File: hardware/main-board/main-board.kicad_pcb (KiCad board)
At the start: 4 copper layers, 77 x 38 mm, 51 parts, among them J1 USB_B_Micro, J2 STDC14, SW1 SW_Push, SW2 SW_Push, U1 TCS3472, U2 STM32L052K6U6, U3 AP2502, U4 USBLC6-2SC6, U5 RT9193

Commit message: Board layout work in progress
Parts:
- removed L1: 600 Ohm, Inductor_SMD:L_0603_1608Metric
- added C14: 1uF, Capacitor_SMD:C_0603_1608Metric, F.Cu at (102.5, 66.9)
- added C15: 1uF, Capacitor_SMD:C_0603_1608Metric, F.Cu at (100.8, 66.9)
- added C16: 1uF, Capacitor_SMD:C_0603_1608Metric, F.Cu at (99.2, 66.9)
- added C17: 1uF, Capacitor_SMD:C_0603_1608Metric, F.Cu at (97.5, 66.9)
- added C18: 0.1uF, Capacitor_SMD:C_0603_1608Metric, F.Cu at (98.0, 56.0)
- added C19: 2.2uF, Capacitor_SMD:C_0603_1608Metric, F.Cu at (86.6, 66.9)
- added C20: 4.7uF, Capacitor_SMD:C_0603_1608Metric, F.Cu at (88.3, 66.9)
- added C21: 0.1uF, Capacitor_SMD:C_0603_1608Metric, F.Cu at (106.0, 56.0)
- added C22: 0.1uF, Capacitor_SMD:C_0603_1608Metric, F.Cu at (131.1, 52.3)
- added C23: 0.1uF, Capacitor_SMD:C_0603_1608Metric, F.Cu at (136.5, 70.6)
- added D10: ESDALC6V1-1U2, lib_fp:ST0201, F.Cu at (109.0, 51.0)
- added D11: ESDALC6V1-1U2, lib_fp:ST0201, F.Cu at (140.2, 71.9)
- added D9: ESDALC6V1-1U2, lib_fp:ST0201, F.Cu at (101.0, 51.0)
- added F1: 250mA, lib_fp:BF_0ZCJ_1206, F.Cu at (134.0, 64.1)
- added FB1: 600R @ 100MHz, Inductor_SMD:L_0603_1608Metric, F.Cu at (129.5, 64.1)
- added FB2: 600R @ 100MHz, Inductor_SMD:L_0603_1608Metric, F.Cu at (163.6, 89.4)
- added J3: Display Connector, lib_fp:ER-CON30HT-1, F.Cu at (95.0, 70.0)
- added J4: Conn_01x02, Connector_JST:JST_SH_BM02B-SRSS-TB_1x02-1MP_P1.00mm_Vertical, F.Cu at (143.4, 50.8)
- added NT1: Net-Tie_2, NetTie:NetTie-2_SMD_Pad0.5mm, F.Cu at (132.5, 46.0)
- added NT2: Net-Tie_2, NetTie:NetTie-2_SMD_Pad0.5mm, F.Cu at (91.2, 67.4)
- added R10: 390K, Resistor_SMD:R_0603_1608Metric, F.Cu at (89.9, 66.9)
- added R11: 100K, Resistor_SMD:R_0603_1608Metric, F.Cu at (100.5, 49.0)
- added R12: 330R, Resistor_SMD:R_0603_1608Metric, F.Cu at (109.0, 56.0)
- added R13: 100K, Resistor_SMD:R_0603_1608Metric, F.Cu at (108.5, 49.0)
- added R14: 330R, Resistor_SMD:R_0603_1608Metric, F.Cu at (136.5, 72.1)
- added R15: 100K, Resistor_SMD:R_0603_1608Metric, F.Cu at (138.8, 71.4)
- added R9: 330R, Resistor_SMD:R_0603_1608Metric, F.Cu at (101.0, 56.0)
- added SW3: SW_Push, lib_fp:ESwitch_TL1105_6mm_H7.5mm, B.Cu at (99.0, 50.0)
- added SW4: SW_Push, lib_fp:ESwitch_TL1105_6mm_H7.5mm, B.Cu at (107.0, 50.0)
- added SW5: SW_Detect, lib_fp:CK_KSU213WLFG, F.Cu at (143.0, 69.0)
- added U6: AP2502, Package_TO_SOT_SMD:SOT-23-6, F.Cu at (130.0, 46.5)
- SW1, SW2: footprint Button_Switch_THT:SW_PUSH_6mm_H5mm -> lib_fp:ESwitch_TL1105_6mm_H7.5mm
- TP2: footprint TestPoint:TestPoint_Keystone_5005-5009_Compact -> TestPoint:TestPoint_Pad_D2.0mm
- U1: value TCS3472 -> TSL2591; footprint lib_fp:AMS_TCS3472_DFN-6 -> lib_fp:AMS_TSL2591
- moved C8 72.1 mm to (162.8, 83.1)
- moved D7 72.1 mm to (173.2, 73.7)
- moved J2 72.1 mm to (175.5, 69.2)
- moved R8 72.1 mm to (166.0, 68.5)
- moved U2 72.1 mm to (167.9, 83.7)
- moved C2 72.1 mm to (162.8, 78.6)
- moved C3 72.1 mm to (162.8, 80.5)
- moved C5 72.1 mm to (162.8, 85.0)
- moved C6 72.1 mm to (162.8, 86.9)
- moved D8 72.1 mm to (175.8, 76.1)
- moved R6 72.1 mm to (166.0, 78.6)
- moved R7 72.1 mm to (166.0, 71.8)
- moved C4 72.1 mm to (173.0, 85.8)
- moved G*** 62.2 mm to (135.1, 108.3)
- moved TP3 39.2 mm to (130.3, 89.0)
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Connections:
- J1 pad 1: +5V -> Net-(F1-Pad2)
- TP1 pad 1: +5V -> Net-(F1-Pad2)
- U1 pad 1: Net-(C1-Pad1) -> /I2C1_SCL
- U1 pad 2: /I2C1_SCL -> Net-(U1-Pad2)
- U1 pad 5: Net-(U1-Pad5) -> Net-(C1-Pad1)
- U2 pad 10: Net-(U2-Pad10) -> /DISP_~CS
- U2 pad 11: Net-(U2-Pad11) -> /DISP_SCK
- U2 pad 12: Net-(U2-Pad12) -> /DISP_D~C
- U2 pad 13: Net-(U2-Pad13) -> /DISP_MOSI
- U2 pad 14: Net-(U2-Pad14) -> /DISP_~RES
- U2 pad 18: Net-(U2-Pad18) -> /BTN5
- U2 pad 25: Net-(U2-Pad25) -> /BTN4
- U2 pad 26: /BTN1 -> /BTN3
- U2 pad 28: Net-(U2-Pad28) -> /BTN1
- U2 pad 8: Net-(U2-Pad8) -> /RLED_EN
- U2 pad 9: /LED_EN -> /TLED_EN
- U3 pad 1: /LED_EN -> /RLED_EN
- U4 pad 5: +5V -> Net-(F1-Pad2)
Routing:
- net Net-(D3-Pad1): track 56.3 -> 0.00 mm
- net /I2C1_SCL: track 60.3 -> 13.4 mm, vias 2 -> 0
- net /I2C1_SDA: track 55.6 -> 11.4 mm, vias 2 -> 0
- net Net-(D2-Pad1): track 38.5 -> 0.00 mm
- net /BTN2: track 27.6 -> 1.40 mm, vias 2 -> 0
- net /LED_EN: track 25.5 -> 0.00 mm
- net /BTN1: track 21.1 -> 1.40 mm, vias 2 -> 0
- net +5V: track 33.2 -> 14.9 mm
- net Net-(D1-Pad1): track 17.7 -> 0.00 mm
- net Net-(D4-Pad1): track 16.5 -> 0.00 mm
- net Net-(F1-Pad2): track 0.00 -> 10.6 mm
- net Net-(D9-Pad1): track 0.00 -> 9.55 mm
- net Net-(D10-Pad1): track 0.00 -> 9.55 mm
- net GND: track 40.6 -> 49.7 mm, vias 33 -> 41
- net Net-(D11-Pad1): track 0.00 -> 5.78 mm
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- removed copper zone on In2.Cu, net +3V3
- removed copper zone on In2.Cu, net +5V
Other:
- board size 77 x 38 mm -> 105 x 38 mm
- board text added: "Rev: A 2021-06-??"
- board text removed: "Reflection Densitometer Probe Development & Test Board"
- board text removed: "Rev: A 2021-03-29"

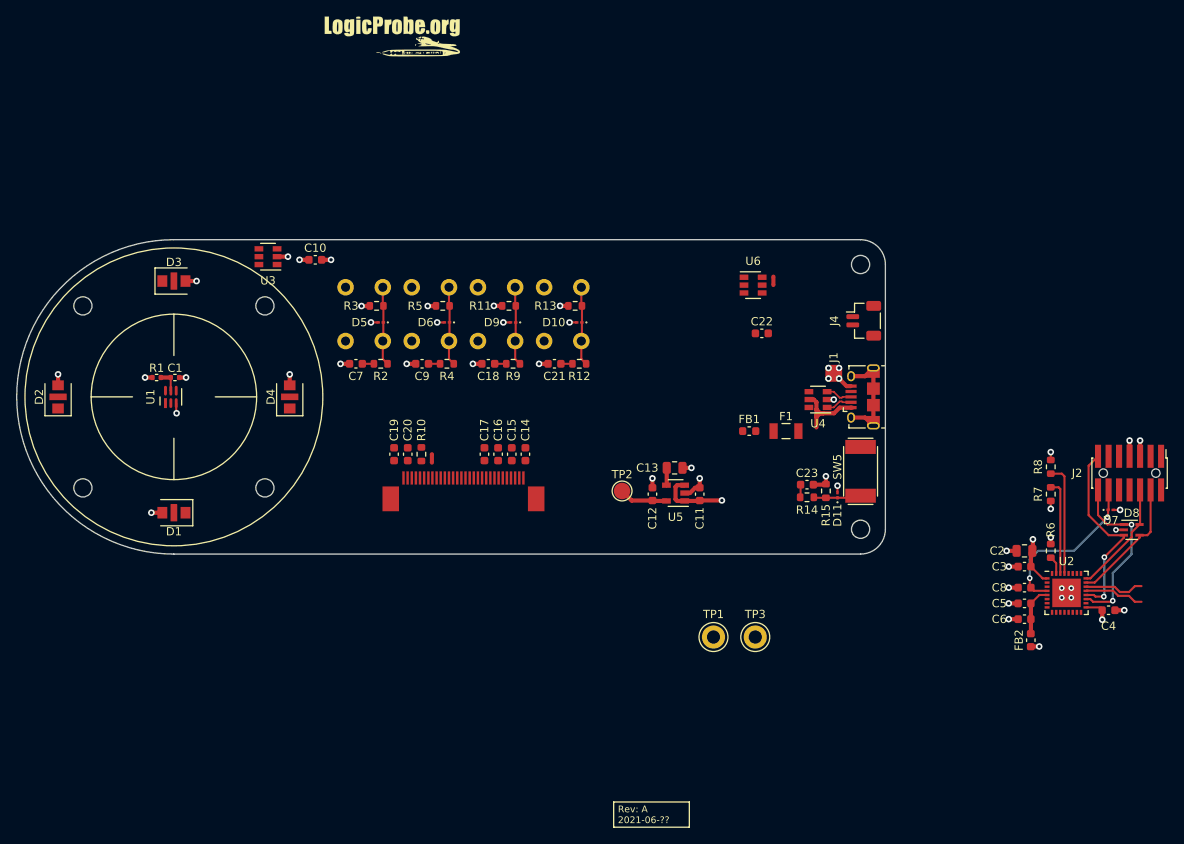
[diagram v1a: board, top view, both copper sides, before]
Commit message: More board layout work
Most components now placed, power and ground planes in place. Many areas
routed, but a lot of inter-section routing work is still TBD.
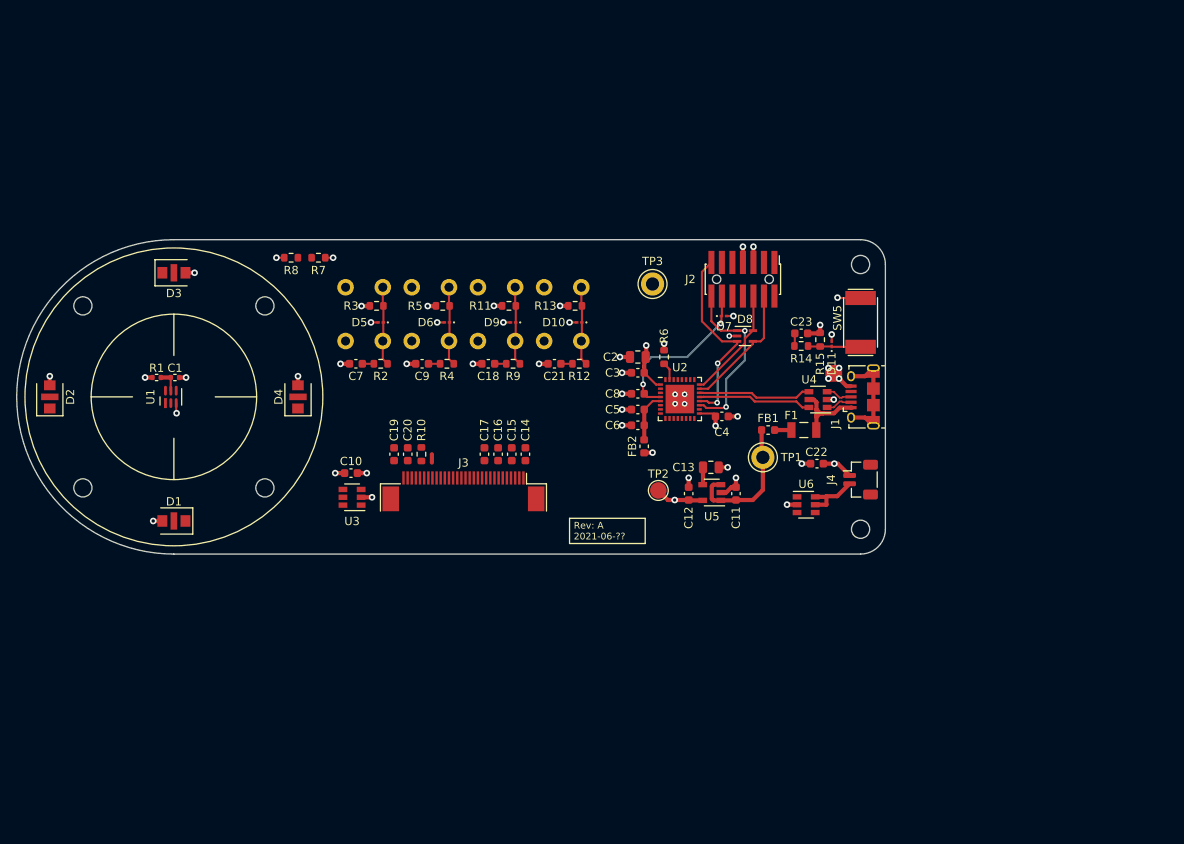
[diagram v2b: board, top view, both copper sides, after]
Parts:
- removed the G*** at (86.4, 16.4)
- moved R8 95.2 mm to (74.2, 43.2), turned to 0 degrees
- moved R7 93.0 mm to (77.5, 43.2), turned to 180 degrees
- moved J2 52.3 mm to (128.8, 45.8)
- moved D7 52.3 mm to (126.5, 50.2)
- moved R6 52.3 mm to (119.3, 55.2)
- moved U2 52.3 mm to (121.2, 60.3)
- moved C2 52.3 mm to (116.1, 55.2)
- moved C3 52.3 mm to (116.1, 57.1)
- moved C4 52.3 mm to (126.2, 62.4)
- moved C8 52.3 mm to (116.1, 59.6)
- moved FB2 52.3 mm to (116.8, 66.0)
- moved C5 52.3 mm to (116.1, 61.5)
- moved C6 52.3 mm to (116.1, 63.4)
- moved D8 52.3 mm to (129.0, 52.6)
- moved TP3 44.4 mm to (117.9, 46.4)
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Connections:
- TP1 pad 1: Net-(F1-Pad2) -> +5V
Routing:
- net /I2C1_SCL: track 13.4 -> 0.00 mm
- net /I2C1_SDA: track 11.4 -> 0.00 mm
- net +5V: track 14.9 -> 26.2 mm
- net /USB_D-: track 7.22 -> 13.8 mm
- net /USB_D+: track 7.22 -> 13.8 mm
- net Net-(J4-Pad2): track 0.00 -> 4.81 mm
- net +3V3: track 19.0 -> 21.8 mm, vias 6 -> 8
- net GND: track 49.7 -> 52.0 mm, vias 41 -> 43
- net Net-(F1-Pad1): track 0.00 -> 2.03 mm
- net Net-(NT1-Pad1): track 0.00 -> 1.36 mm
- net Net-(D11-Pad1): track 5.78 -> 6.39 mm
- added copper zone on In2.Cu, net +3V3
- added copper zone on In2.Cu, net +5V

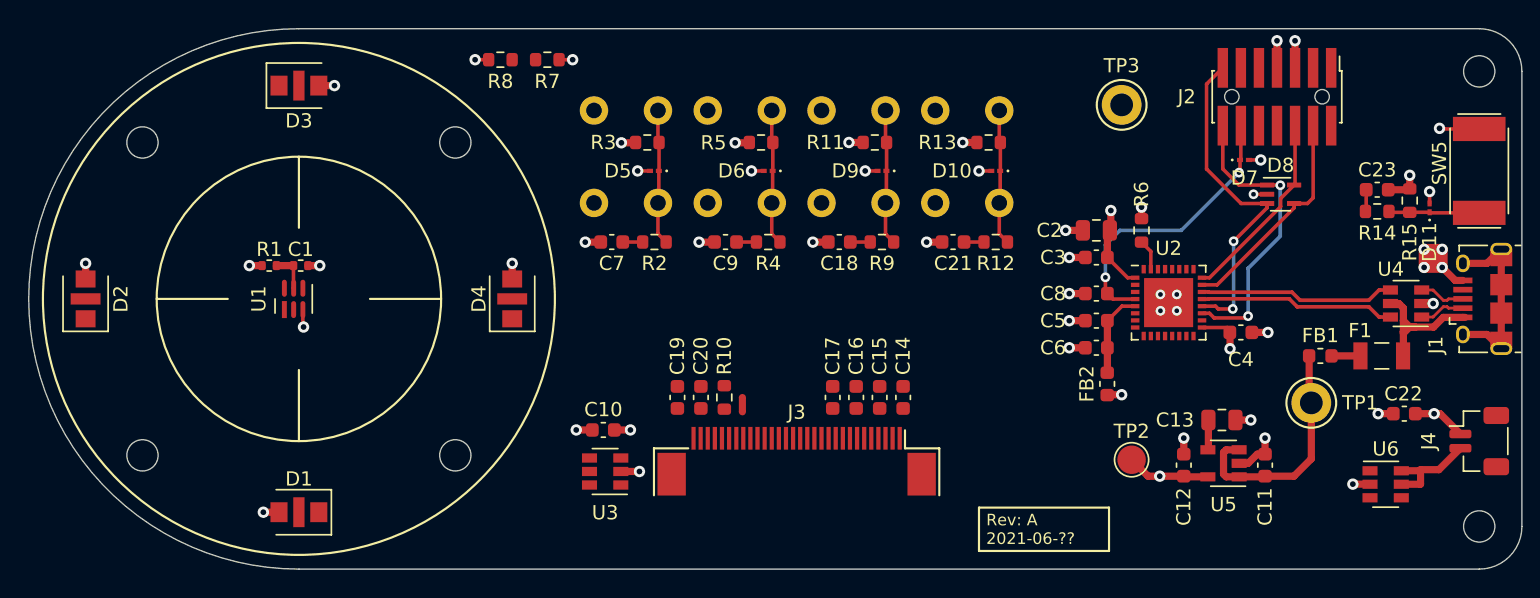
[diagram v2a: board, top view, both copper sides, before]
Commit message: First pass at layout complete, still needs cleanup
All the display lines should be redone. The button and I2C lines may be
okay, but have room for improvement. Hopefully all the mechanical
aspects are mostly frozen until a CAD model of the enclosure is built.
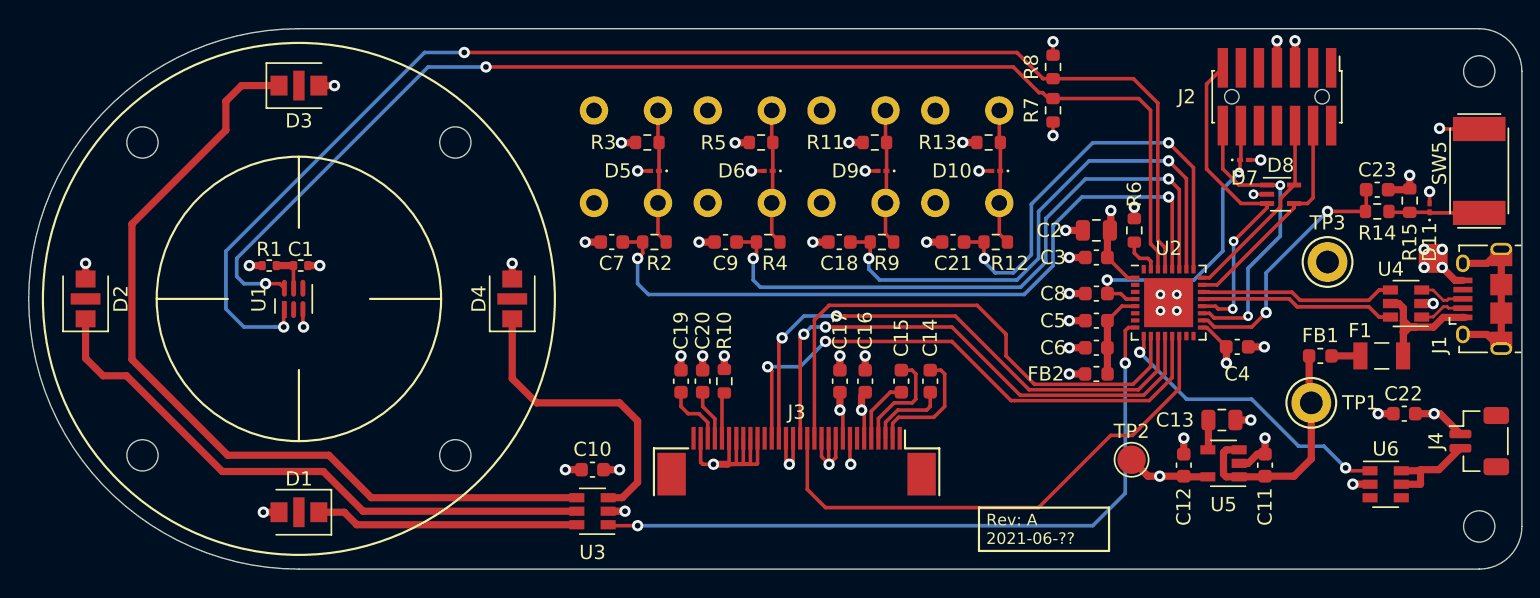
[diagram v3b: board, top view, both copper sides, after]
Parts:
- moved R8 38.9 mm to (113.0, 43.7), turned to 270 degrees
- moved R7 35.7 mm to (113.0, 46.7), turned to 90 degrees
- moved TP3 18.2 mm to (132.3, 57.4)
- moved NT2 4.46 mm to (89.7, 71.6), turned to 180 degrees
- moved U3 2.93 mm to (80.6, 74.9)
- moved C10 2.90 mm to (80.6, 72.0)
- moved C14 2.22 mm to (104.4, 65.8), turned to 270 degrees
- moved C15 1.91 mm to (102.4, 65.8), turned to 270 degrees
- moved C16 1.31 mm to (99.8, 65.8)
- moved C17 1.25 mm to (98.0, 65.8)
- moved C19 1.17 mm to (86.9, 65.8)
- moved C20 1.15 mm to (88.4, 65.8)
- moved R10 1.14 mm to (89.9, 65.8)
- moved C4 1.05 mm to (126.0, 63.4)
- moved FB2 1.03 mm to (116.1, 65.3), turned to 0 degrees
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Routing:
- net /I2C1_SCL: track 0.00 -> 94.6 mm, vias 0 -> 2
- net /I2C1_SDA: track 0.00 -> 87.5 mm, vias 0 -> 2
- net Net-(D3-Pad1): track 0.00 -> 60.4 mm
- net /BTN1: track 1.40 -> 51.9 mm, vias 0 -> 2
- net /RLED_EN: track 0.00 -> 49.6 mm, vias 0 -> 2
- net /BTN2: track 1.40 -> 45.2 mm, vias 0 -> 2
- net Net-(D2-Pad1): track 0.00 -> 41.8 mm
- net /DISP_MOSI: track 0.00 -> 39.6 mm, vias 0 -> 2
- net /DISP_SCK: track 0.00 -> 39.3 mm, vias 0 -> 2
- net /DISP_D~C: track 0.00 -> 38.3 mm, vias 0 -> 2
- net /DISP_~CS: track 0.00 -> 38.3 mm
- net /DISP_~RES: track 0.00 -> 37.4 mm
- net /BTN3: track 1.40 -> 38.3 mm, vias 0 -> 2
- net /BTN4: track 1.40 -> 31.6 mm, vias 0 -> 2
- net Net-(D4-Pad1): track 0.00 -> 21.1 mm
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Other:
- board text added: "Clean up routing of display lines"

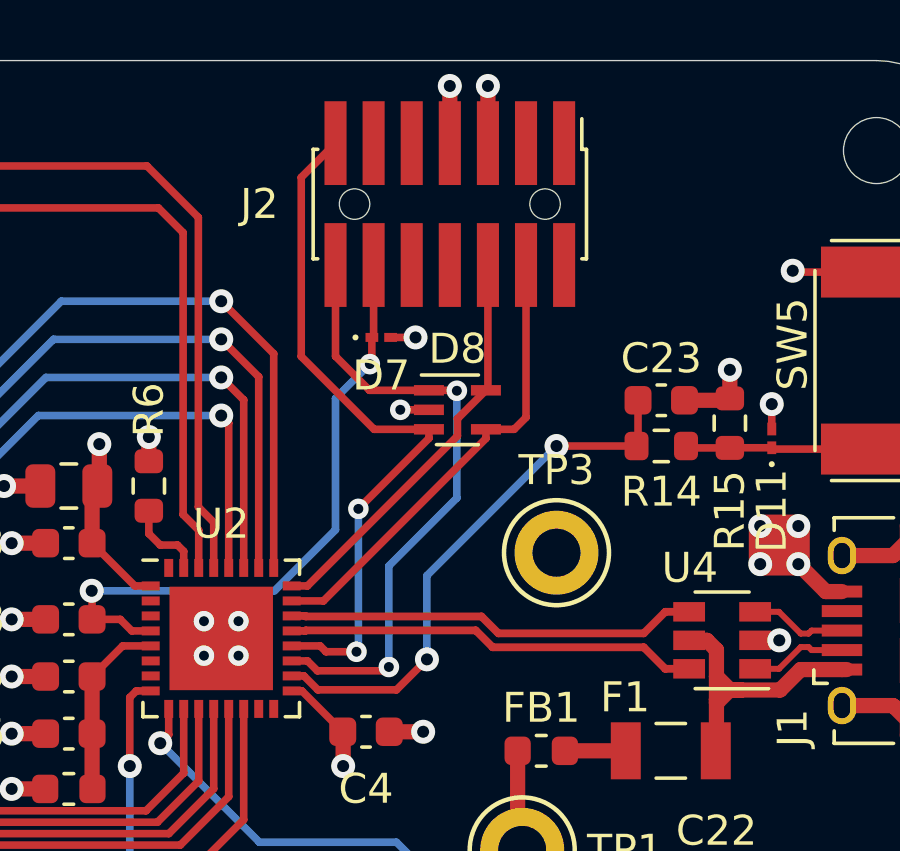
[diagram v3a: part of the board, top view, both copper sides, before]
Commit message: Switched debug connector to a Tag-Connect TC2070
This makes it easier to put on the opposite side of the board, where it
won't be obstructed.
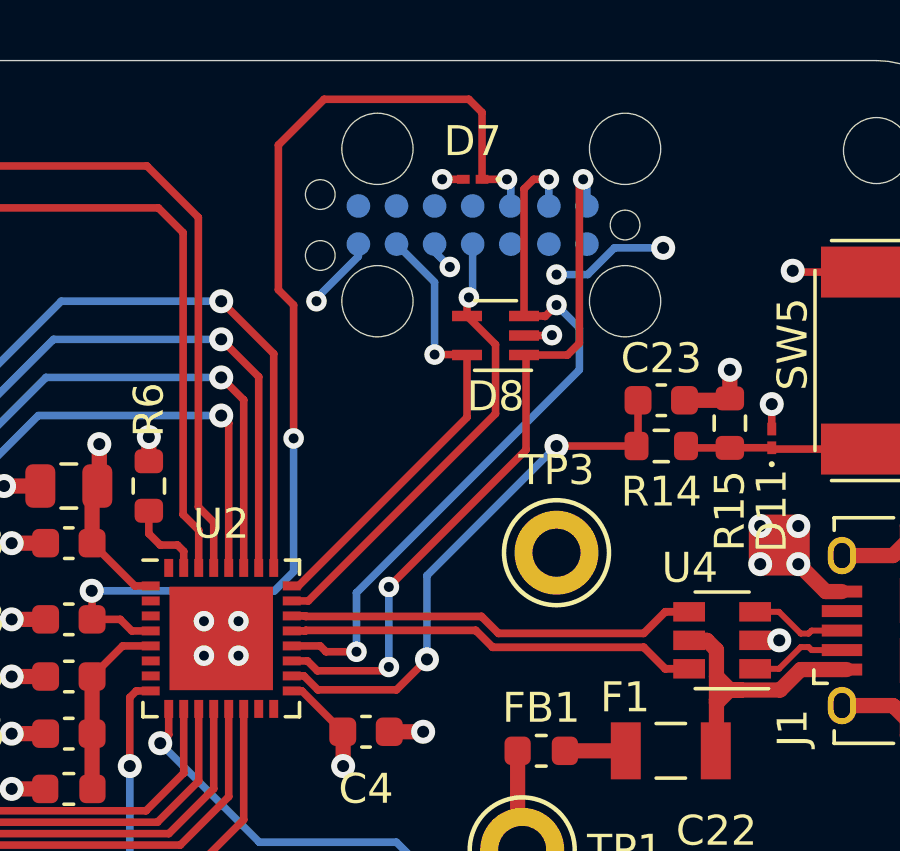
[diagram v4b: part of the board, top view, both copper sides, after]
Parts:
- removed the G*** at (131.3, 45.2)
- J2: value STDC14 -> DNI; footprint lib_fp:Samtec_FTSH-107-01-L-DV-K-A_2x07_P1.27mm -> Connector:Tag-Connect_TC2070-IDC-FP_2x07_P1.27mm_Vertical; moved to B.Cu
- moved D7 6.09 mm to (129.5, 45.0), turned to 180 degrees
- moved D8 2.78 mm to (130.3, 50.2), turned to 180 degrees
- moved J2 1.03 mm to (129.5, 46.5)
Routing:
- net /RESET: track 21.4 -> 36.1 mm, vias 2 -> 3
- net GND: track 71.1 -> 74.5 mm, vias 52 -> 54
- net /USART1_TX: track 21.0 -> 24.1 mm, vias 2 -> 3
- net /SWCLK: track 13.6 -> 15.5 mm, vias 0 -> 1
- net /USART1_RX: track 23.4 -> 24.4 mm, vias 2 -> 3
- net /SWDIO: vias 0 -> 1
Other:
- board text added: "TC2070"
